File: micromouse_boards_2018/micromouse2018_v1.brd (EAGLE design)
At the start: 160 x 100 mm, 35 parts

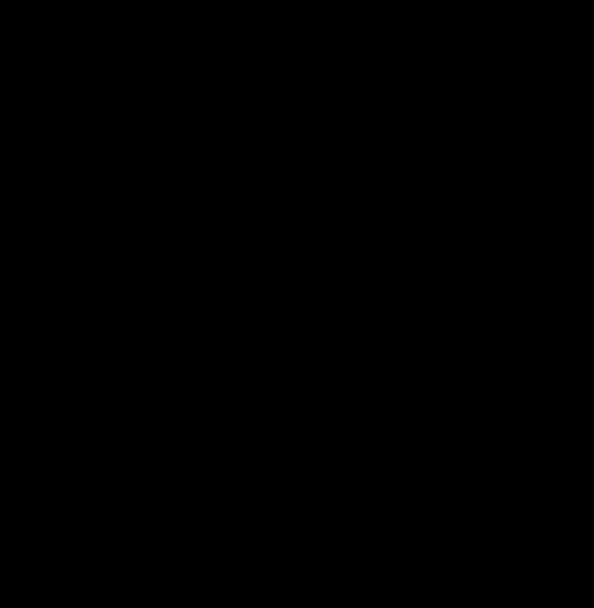
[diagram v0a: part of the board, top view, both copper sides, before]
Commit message: Added power switch to schematic
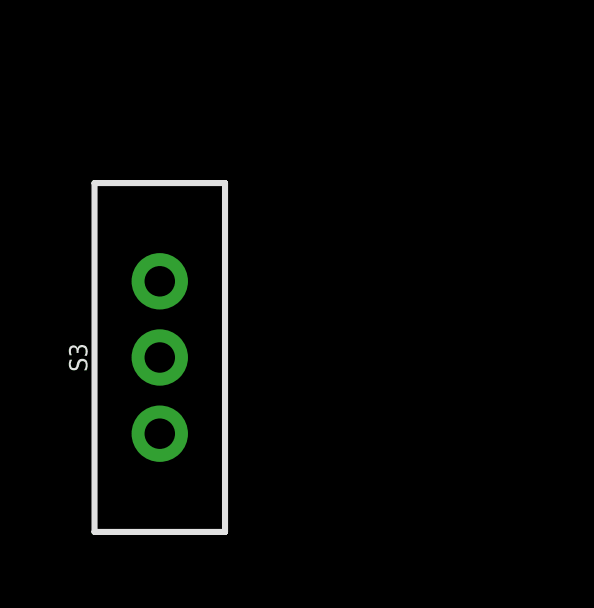
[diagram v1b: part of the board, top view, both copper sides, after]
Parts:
- added S3: (no value), SparkFun-Switches:SWITCH_SPDT_PTH_11.6X4.0MM
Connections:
- net V_BATT: now also S3.3
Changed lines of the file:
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@@
 <element name="U$3" library="raParts" package="1X04_SMD_VERTICAL_COMBO" value="ULTRASONIC" x="-22.86" y="64.77"/>
 <element name="U$4" library="raParts" package="1X04_SMD_VERTICAL_COMBO" value="ULTRASONIC" x="-34.29" y="64.77"/>
+<element name="S3" library="SparkFun-Switches" package="SWITCH_SPDT_PTH_11.6X4.0MM" value="" x="-110.49" y="6.35">
+<attribute name="PROD_ID" value="SWCH-08261" x="-110.49" y="6.35" size="1.778" layer="27" display="off"/>
+<attribute name="SF_SKU" value="COM-00102" x="-110.49" y="6.35" size="1.778" layer="27" display="off"/>
+</element>
 </elements>
 <signals>
@@
 <signal name="V_BATT">
 <contactref element="D1" pad="C"/>
+<contactref element="S3" pad="3"/>
+<wire x1="-41.033" y1="76.2" x2="-110.49" y2="3.81" width="0" layer="19" extent="1-1"/>
 </signal>
 <signal name="12V">

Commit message: Added power circuit
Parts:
- added C10: 15u, resistor:C0805
- added C6: 680p, resistor:C0805
- added C7: 15p, resistor:C0805
- added C8: 22u, rcl:C1210
- added C9: 0.1u, resistor:C0805
- added D5: SS13FL, Scraps:SODFL3617X108N
- added IC1: TPS562210DDFT, TPS562210DDFT:SOT65P280X110-8N
- added R13: 39.2k, resistor:R0805
- added R14: 10.2k, resistor:R0805
- added R15: 732, resistor:R0805
- added U$10: 22u, AcceleratedDesigns_Lib:1210
- added U$11, U$7: SRN6045-4R7Y, AcceleratedDesigns_Lib:SRN6045
- added U$12: 100k, AcceleratedDesigns_Lib:0805
- added U$13: 56.2k, AcceleratedDesigns_Lib:0805
- added U$14: 10.2k, AcceleratedDesigns_Lib:0805
- added U$15: 22u, AcceleratedDesigns_Lib:1206_190
- added U$5: TPS54332, TPS54332:DDA8_2P13X3-M
- added U$6: 8.20n\, AcceleratedDesigns_Lib:1206
- added U$8: 0.1u, AcceleratedDesigns_Lib:0805
- added U$9: 8.2n, AcceleratedDesigns_Lib:1206
- moved S3 39.4 mm to (-71.1, 6.35)
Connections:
- new net N$10: C9.1, U$5.1
- new net N$11: C7.1, R13.2, U$5.6
- new net N$12: C6.1, R13.1
- new net N$15: IC1.4, U$12.2
- new net N$16: IC1.6, U$13.2, U$14.1
- new net N$18: IC1.5, U$9.1
- new net N$19: C8.1, IC1.3, IC1.7, S3.2, U$10.1, U$5.2
- new net N$5: U$5.4, U$6.2
- new net N$6: IC1.8, U$8.2
- new net N$7: C9.2, D5.1, U$5.8, U$7.1
- new net N$8: IC1.2, U$11.1, U$8.1
- new net N$9: R14.1, R15.2, U$5.5
- net 12V: now also C10.1, R14.2, U$7.2
- net 5V: now also U$11.2, U$12.1, U$13.1, U$15.1
- net GND: now also C10.2, C6.2, C7.2, C8.2, D5.2, IC1.1, R15.1, S3.1, U$10.2, U$14.2, U$15.2, U$5.7, U$5.EPAD, U$6.1, U$9.2
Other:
- board size 160 x 100 mm -> 100 x 80 mm

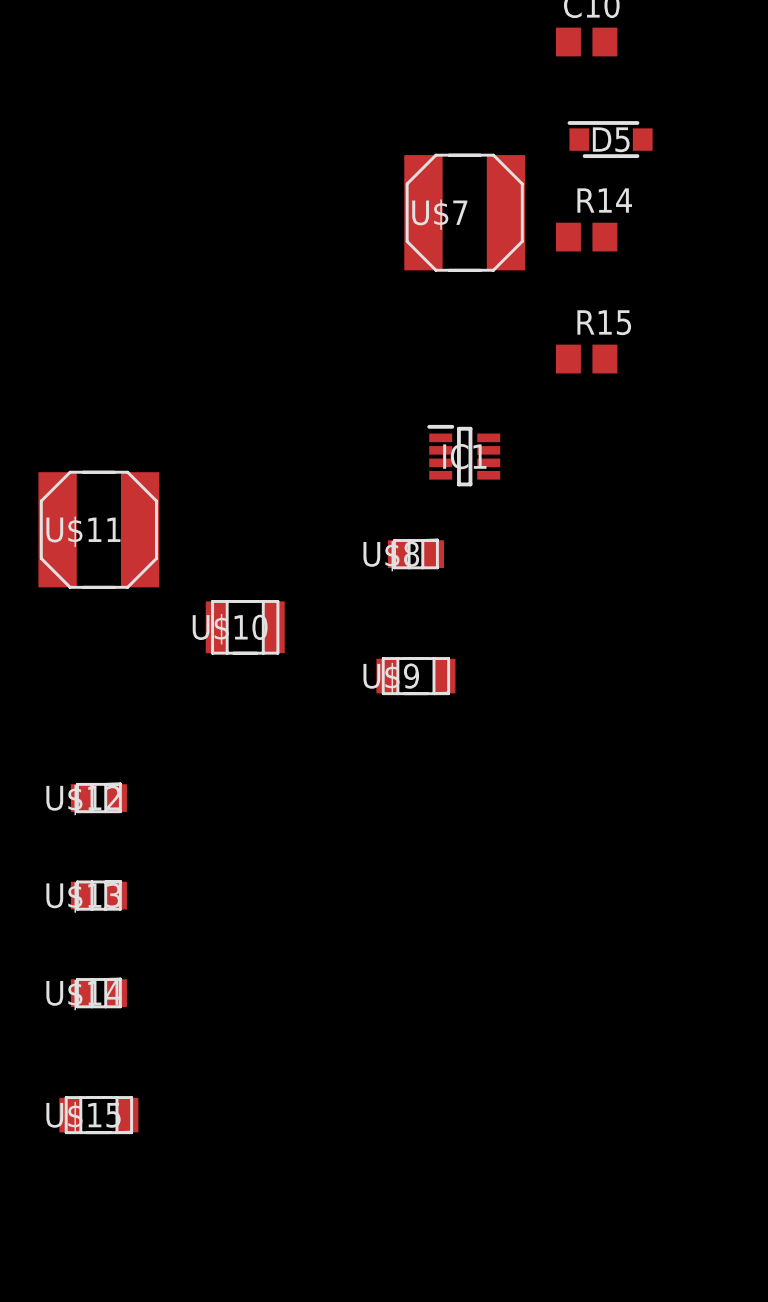
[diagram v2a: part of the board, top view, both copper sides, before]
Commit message: Changed SS31FL diode to CMS06 for better heat dissipation
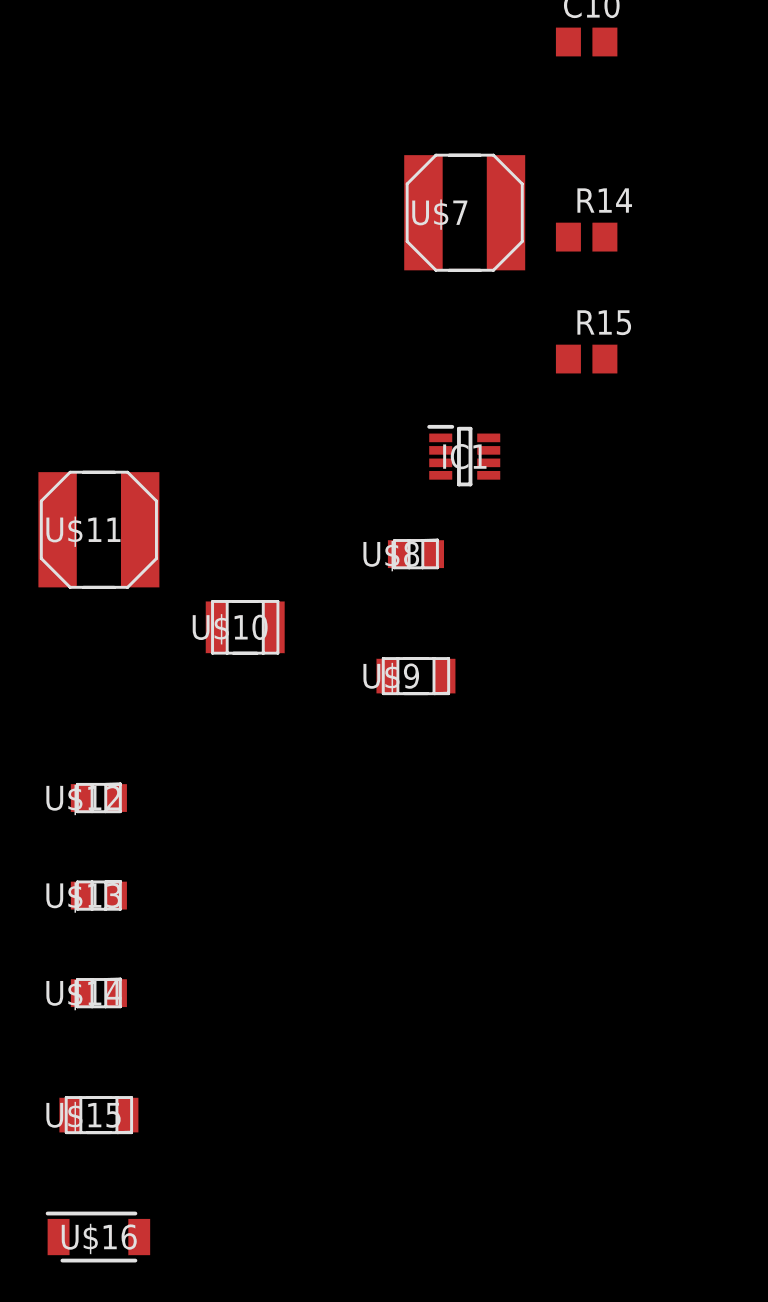
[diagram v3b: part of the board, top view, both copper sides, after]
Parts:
- removed D5: SS13FL, Scraps:SODFL3617X108N
- added U$16: CMS06, Scraps:SODFL4724X108N
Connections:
- net GND: now also U$16.1; no longer D5.2
- net N$7: now also U$16.2; no longer D5.1
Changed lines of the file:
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@@
 <element name="C9" library="resistor" library_urn="urn:adsk.eagle:library:348" package="C0805" package3d_urn="urn:adsk.eagle:package:26137/1" value="0.1u" x="-106.68" y="-114.3"/>
 <element name="C10" library="resistor" library_urn="urn:adsk.eagle:library:348" package="C0805" package3d_urn="urn:adsk.eagle:package:26137/1" value="15u" x="-106.68" y="-120.65"/>
-<element name="D5" library="Scraps" package="SODFL3617X108N" value="SS13FL" x="-105.41" y="-125.73">
-<attribute name="DESCRIPTION" value="Schottky Diodes &amp; Rectifiers 30V, 1A SCHOTTKY" x="-105.41" y="-125.73" size="1.778" layer="27" display="off"/>
-<attribute name="HEIGHT" value="1.08mm" x="-105.41" y="-125.73" size="1.778" layer="27" display="off"/>
-<attribute name="MANUFACTURER_NAME" value="Fairchild Semiconductor" x="-105.41" y="-125.73" size="1.778" layer="27" display="off"/>
-<attribute name="MANUFACTURER_PART_NUMBER" value="SS13FL" x="-105.41" y="-125.73" size="1.778" layer="27" display="off"/>
-<attribute name="RS_PART_NUMBER" value="" x="-105.41" y="-125.73" size="1.778" layer="27" display="off"/>
-<attribute name="RS_PRICE/STOCK" value="" x="-105.41" y="-125.73" size="1.778" layer="27" display="off"/>
-</element>
 <element name="R14" library="resistor" library_urn="urn:adsk.eagle:library:348" package="R0805" package3d_urn="urn:adsk.eagle:package:26059/1" value="10.2k" x="-106.68" y="-130.81"/>
 <element name="R15" library="resistor" library_urn="urn:adsk.eagle:library:348" package="R0805" package3d_urn="urn:adsk.eagle:package:26059/1" value="732" x="-106.68" y="-137.16"/>
@@
 <attribute name="VENDOR" value="MuRata" x="-132.08" y="-176.53" size="1.778" layer="27" display="off"/>
 </element>
+<element name="U$16" library="Scraps" package="SODFL4724X108N" value="CMS06" x="-132.08" y="-182.88"/>
 </elements>
 <signals>
@@
 <contactref element="J3" pad="2"/>
 <contactref element="J4" pad="2"/>
-<contactref element="D5" pad="2"/>
 <contactref element="R15" pad="1"/>
 <contactref element="U$5" pad="7"/>
@@
 <contactref element="S3" pad="1"/>
 <contactref element="U$5" pad="EPAD"/>
+<contactref element="U$16" pad="1"/>
 <wire x1="-107.63" y1="-137.16" x2="-114.28" y2="-141.265" width="0" layer="19" extent="1-1"/>
-<wire x1="-103.76" y1="-125.73" x2="-107.63" y2="-137.16" width="0" layer="19" extent="1-1"/>
-<wire x1="-105.73" y1="-120.65" x2="-103.76" y2="-125.73" width="0" layer="19" extent="1-1"/>
 <wire x1="-114.0714" y1="-153.67" x2="-114.28" y2="-141.265" width="0" layer="19" extent="1-1"/>
 <wire x1="-122.9614" y1="-151.13" x2="-114.0714" y2="-153.67" width="0" layer="19" extent="1-1"/>
+<wire x1="-105.73" y1="-120.65" x2="-107.63" y2="-137.16" width="0" layer="19" extent="1-1"/>
 <wire x1="-105.28" y1="-105.41" x2="-105.73" y2="-120.65" width="0" layer="19" extent="1-1"/>
 <wire x1="-96.84" y1="-101.6" x2="-105.28" y2="-105.41" width="0" layer="19" extent="1-1"/>
@@
 <wire x1="-131.1783" y1="-170.18" x2="-122.9614" y2="-151.13" width="0" layer="19" extent="1-1"/>
 <wire x1="-130.5814" y1="-176.53" x2="-131.1783" y2="-170.18" width="0" layer="19" extent="1-1"/>
+<wire x1="-134.18" y1="-182.88" x2="-130.5814" y2="-176.53" width="0" layer="19" extent="1-1"/>
 <wire x1="-65.9" y1="5.13" x2="-92.6338" y2="-80.645" width="0" layer="19" extent="1-1"/>
 <wire x1="-71.12" y1="8.89" x2="-65.9" y2="5.13" width="0" layer="19" extent="1-1"/>
@@
 <contactref element="U$5" pad="8"/>
 <contactref element="U$7" pad="1"/>
-<contactref element="D5" pad="1"/>
-<wire x1="-107.06" y1="-125.73" x2="-115.18" y2="-129.54" width="0" layer="19" extent="1-1"/>
-<wire x1="-105.73" y1="-114.3" x2="-107.06" y2="-125.73" width="0" layer="19" extent="1-1"/>
+<contactref element="U$16" pad="2"/>
+<wire x1="-105.73" y1="-114.3" x2="-115.18" y2="-129.54" width="0" layer="19" extent="1-1"/>
 <wire x1="-92.6338" y1="-79.375" x2="-105.73" y2="-114.3" width="0" layer="19" extent="1-1"/>
+<wire x1="-129.98" y1="-182.88" x2="-115.18" y2="-129.54" width="0" layer="19" extent="1-1"/>
 </signal>
 <signal name="N$9">

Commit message: Rough draft for 5V power circuit layout
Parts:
- moved U$16 282.7 mm to (18.9, 56.1)
- moved U$15 254.2 mm to (21.5, 26.1), turned to 270 degrees
- moved U$14 249.8 mm to (37.9, 12.8)
- moved U$7 243.4 mm to (34.0, 64.5)
- moved U$13 242.0 mm to (37.1, 7.92), turned to 90 degrees
- moved U$11 237.7 mm to (32.0, 25.9), turned to 90 degrees
- moved R15 233.6 mm to (33.3, 49.8)
- moved U$12 233.4 mm to (30.0, 7.92), turned to 90 degrees
- moved R14 233.0 mm to (32.3, 56.2)
- moved C10 229.4 mm to (39.3, 56.4)
- moved U$8 227.2 mm to (40.7, 17.6), turned to 270 degrees
- moved U$9 219.5 mm to (33.3, 7.57), turned to 270 degrees
- moved U$10 218.8 mm to (19.5, 13.7), turned to 90 degrees
- moved C9 215.1 mm to (26.3, 54.7)
- moved IC1 213.7 mm to (32.0, 14.8)
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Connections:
- net N$19 renamed VIN
- net N$8 renamed BOOT
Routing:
- net 5V: track 0.00 -> 63.0 mm, vias 0 -> 2
- net GND: track 0.00 -> 41.6 mm, vias 0 -> 20
- net VIN: track 0.00 -> 25.8 mm, vias 0 -> 2
- net BOOT: track 0.00 -> 17.7 mm, vias 0 -> 6
- net N$16: track 0.00 -> 8.50 mm
- net N$6: track 0.00 -> 7.85 mm
- net N$15: track 0.00 -> 5.25 mm
- net N$18: track 0.00 -> 4.76 mm
- added copper zone on layer 1, net 5V
- added copper zone on layer 1, net BOOT
- added copper zone on layer 1, net GND
- added copper zone on layer 16, net GND
- added copper zone on layer 1, net VIN

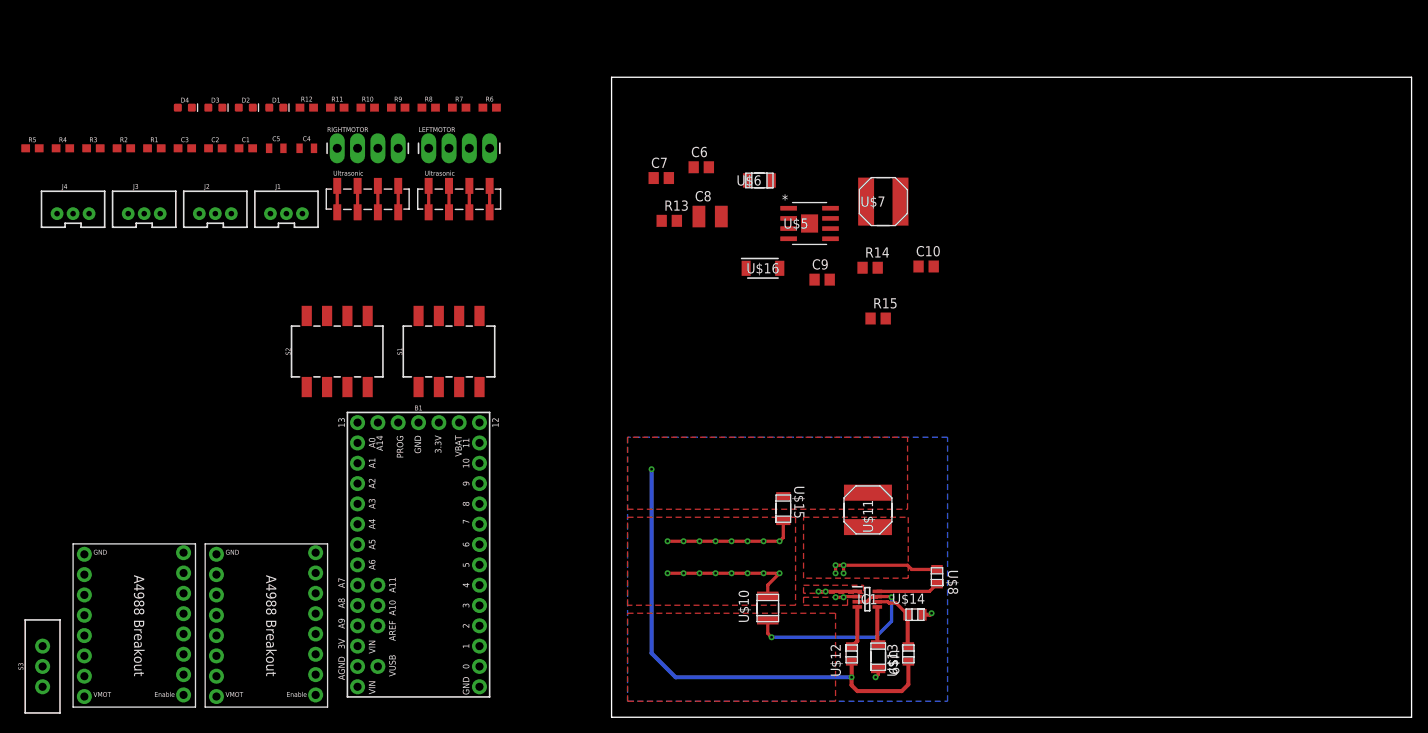
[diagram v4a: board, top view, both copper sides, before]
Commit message: Created 12V layout, removed thermals on 5V layout
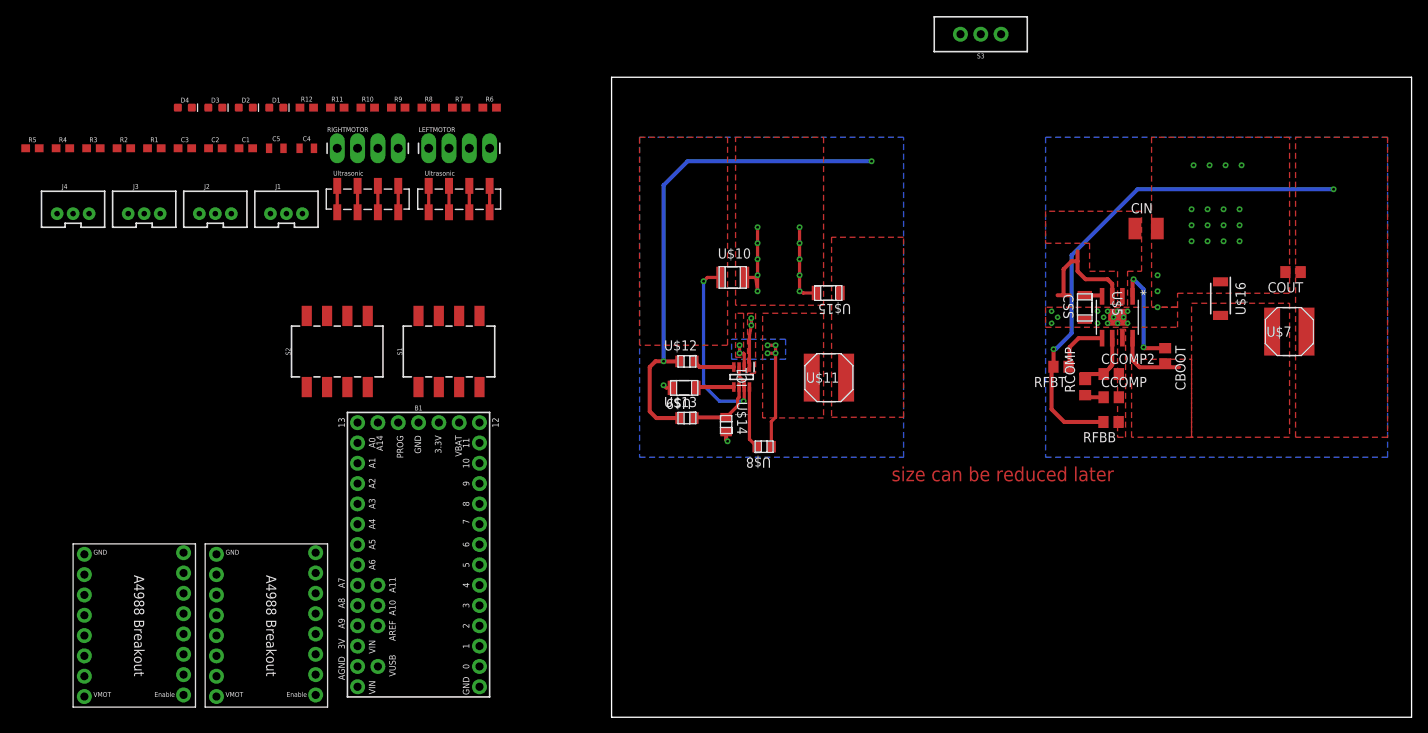
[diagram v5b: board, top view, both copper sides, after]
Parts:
- removed C10: 15u, resistor:C0805
- removed C6: 680p, resistor:C0805
- removed C7: 15p, resistor:C0805
- removed C8: 22u, rcl:C1210
- removed C9: 0.1u, resistor:C0805
- removed R13: 39.2k, resistor:R0805
- removed R14: 10.2k, resistor:R0805
- removed R15: 732, resistor:R0805
- removed U$6: 8.20n\, AcceleratedDesigns_Lib:1206
- added CBOOT: 0.1u, resistor:C0805
- added CCOMP: 680p, resistor:C0805
- added CCOMP2: 15p, resistor:C0805
- added CIN: 22u, rcl:C1210
- added COUT: 15u, resistor:C0805
- added CSS: 8.20n\, AcceleratedDesigns_Lib:1206
- added RCOMP: 39.2k, resistor:R0805
- added RFBB: 732, resistor:R0805
- added RFBT: 10.2k, resistor:R0805
- moved S3 141.4 mm to (46.1, 85.4), turned to 90 degrees
- moved U$16 57.3 mm to (76.1, 52.3), turned to 270 degrees
- moved U$7 53.3 mm to (84.7, 48.2)
- moved U$12 42.0 mm to (9.42, 44.5), turned to 0 degrees
- moved U$10 41.6 mm to (15.2, 55.0), turned to 0 degrees
- moved U$9 41.4 mm to (9.07, 41.2), turned to 180 degrees
- moved U$13 40.4 mm to (9.42, 37.4), turned to 0 degrees
- moved U$5 40.2 mm to (63.2, 50.0), turned to 270 degrees
- moved U$14 33.5 mm to (14.3, 36.6), turned to 270 degrees
- moved IC1 31.9 mm to (16.3, 42.5), turned to 270 degrees
- moved U$15 27.5 mm to (27.1, 53.0), turned to 180 degrees
- moved U$8 27.0 mm to (19.1, 33.8), turned to 180 degrees
- moved U$11 17.2 mm to (27.2, 42.5), turned to 0 degrees
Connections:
- removed net N$7: C9.2, U$16.2, U$5.8, U$7.1
- new net N$8: U$5.3
- new net PH: CBOOT.2, U$16.2, U$5.8, U$7.1
- net 12V: now also COUT.1, RFBT.2; no longer C10.1, R14.2
- net GND: now also CCOMP.2, CCOMP2.2, CIN.2, COUT.2, CSS.1, RFBB.1; no longer C10.2, C6.2, C7.2, C8.2, R15.1, U$6.1
- net N$10: now also CBOOT.1; no longer C9.1
- net N$11: now also CCOMP2.1, RCOMP.2; no longer C7.1, R13.2
- net N$12: now also CCOMP.1, RCOMP.1; no longer C6.1, R13.1
- net N$5: now also CSS.2; no longer U$6.2
- net N$9: now also RFBB.2, RFBT.1; no longer R14.1, R15.2
- net VIN: now also CIN.1; no longer C8.1
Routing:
- net 12V: track 0.00 -> 50.9 mm, vias 0 -> 2
- net N$9: track 0.00 -> 19.1 mm
- net N$8: track 0.00 -> 16.0 mm
- net N$10: track 0.00 -> 14.0 mm, vias 0 -> 2
- net GND: track 41.6 -> 29.8 mm, vias 20 -> 47
- net PH: track 0.00 -> 8.93 mm
- net N$11: track 0.00 -> 8.65 mm
- net N$12: track 0.00 -> 2.42 mm
- net N$5: track 0.00 -> 2.21 mm
- added copper zone on layer 1, net 12V
- added copper zone on layer 16, net BOOT
- added copper zone on layer 1, net PH
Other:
- board text added: "size can be reduced later"
